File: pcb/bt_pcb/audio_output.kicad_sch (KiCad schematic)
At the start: 34 parts, among them IC1 ADG736BRM, IC2 ADG736BRM, J3 AudioJack3_Switch, J7 AudioJack3_Switch, U2 MCP6004, U4 MCP6004

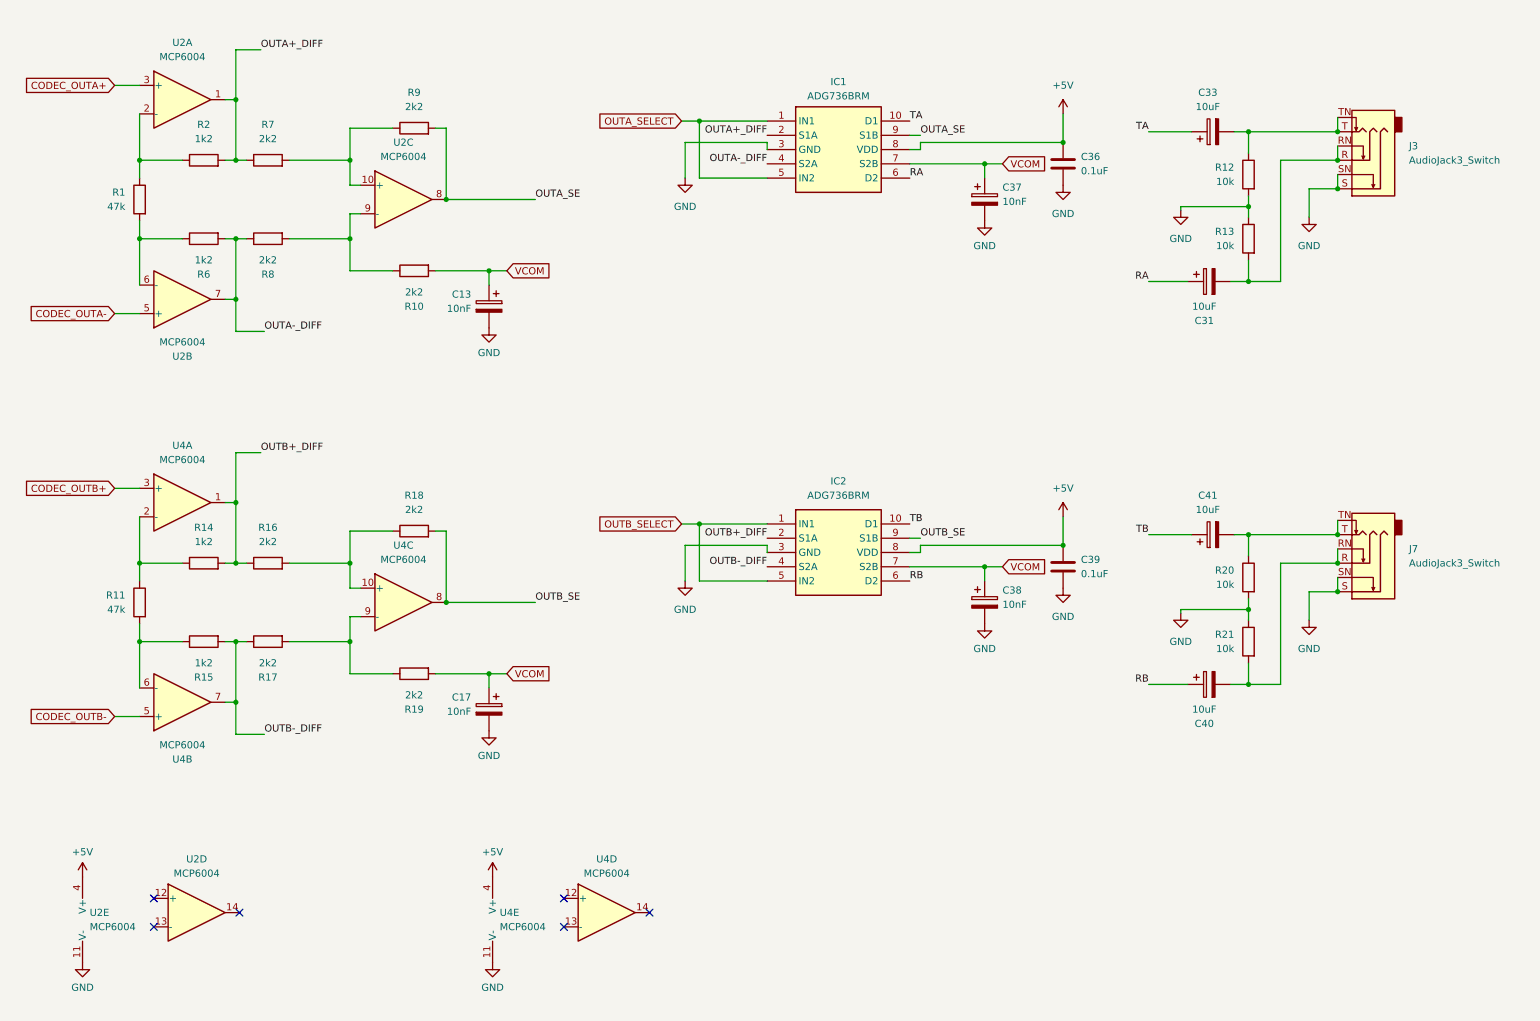
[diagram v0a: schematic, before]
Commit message: ditching power pcb, new codec
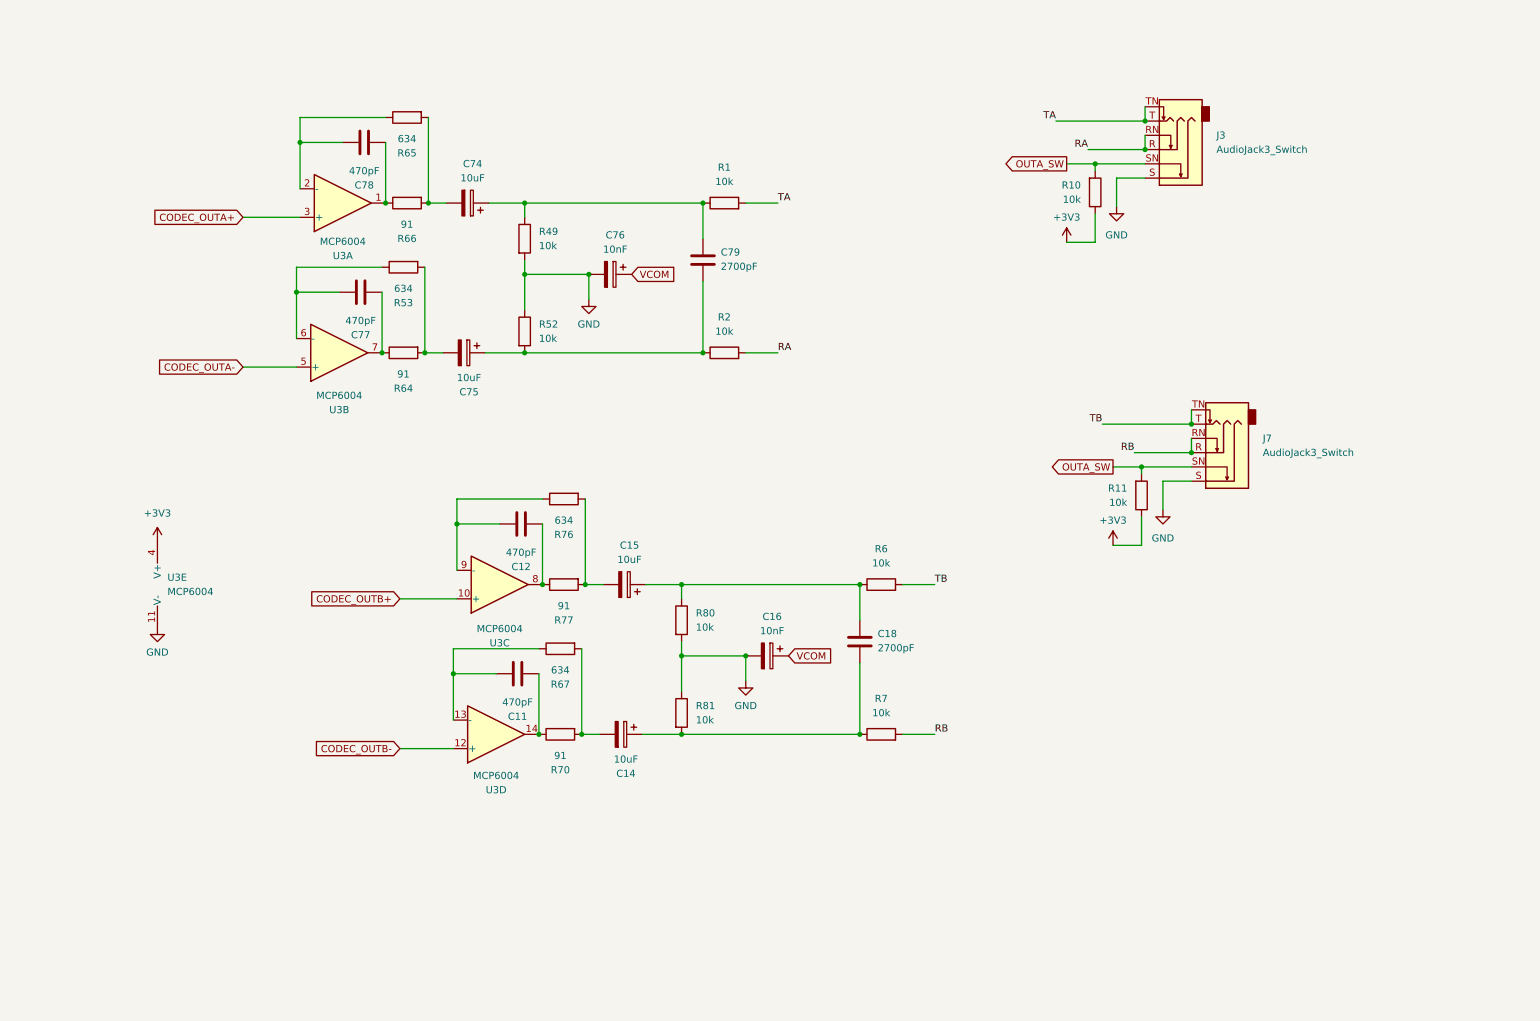
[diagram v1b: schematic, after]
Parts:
- removed C13, C17, C37, C38: 10nF, symbol Device:C_Polarized
- removed C31, C33, C40, C41: 10uF, symbol Device:C_Polarized
- removed C36, C39: 0.1uF, symbol Device:C
- removed IC1, IC2: ADG736BRM, library:SOP50P490X110-10N, symbol library:ADG736BRM
- removed R12, R13, R20, R21: 10k, symbol Device:R
- removed R14, R15: 1k2, symbol Device:R
- removed R16, R17, R18, R19, R8, R9: 2k2, symbol Device:R
- removed U2, U4: MCP6004, symbol Amplifier_Operational:MCP6004
- added C11, C12, C77, C78: 470pF, symbol Device:C
- added C14, C15, C74, C75: 10uF, symbol Device:C_Polarized
- added C16, C76: 10nF, symbol Device:C_Polarized
- added C18, C79: 2700pF, symbol Device:C
- added R49, R52, R80, R81: 10k, symbol Device:R
- added R53, R65, R67, R76: 634, symbol Device:R
- added R64, R66, R70, R77: 91, symbol Device:R
- added U3: MCP6004, symbol Amplifier_Operational:MCP6004
- R1, R11: value 47k -> 10k
- R10, R7: value 2k2 -> 10k
- R2, R6: value 1k2 -> 10k
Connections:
- net OUTA-_DIFF is gone; now on net TB: R6.2
- net CODEC_OUTA+: now also U3.3 (+)
- net CODEC_OUTA-: now also U3.5 (+)
- net CODEC_OUTB+: now also U3.10 (+)
- net CODEC_OUTB-: now also U3.12 (+)
- net GND: now also C16.2, C76.2, R49.2, R52.1, R80.2, R81.1, U3.11 (V-); no longer J3.SN, J7.SN
- net RA: now also J3.R, J3.RN, R2.2
- net RB: now also J7.R, J7.RN, R7.2
- net TA: now also J3.T, J3.TN, R1.2
- net TB: now also J7.T, J7.TN
- net VCOM: now also C16.1, C76.1; no longer R10.2
- net +3V3: now reaches R11.1
- net +3V3: now also R10.1, U3.4 (V+)
- net at R1.1: now also C74.1, C79.1, R49.1; no longer R2.1
- net OUTA_SW: now reaches R11.2
- net OUTA_SW: now also J3.SN, J7.SN, R10.2
- net at R6.1: now also C15.1, C18.1, R80.1; no longer R1.2
- net OUTA+_DIFF: no longer names the net of R7.1
- net OUTA+_DIFF: now also C14.1, C18.2, R81.2; no longer R2.2
- new net: C74.2, R65.2, R66.2
- new net: C77.1, R64.1, U3.7
- new net: C75.2, R53.2, R64.2
- new net: C12.1, R77.1, U3.8
- new net: C12.2, R76.1, U3.9 (-)
- new net: C75.1, C79.2, R2.1, R52.2
- new net: C11.1, R70.1, U3.14
- new net: C11.2, R67.1, U3.13 (-)
- new net: C15.2, R76.2, R77.2
- new net: C14.2, R67.2, R70.2
- new net: C78.1, R66.1, U3.1
- new net: C78.2, R65.1, U3.2 (-)
- new net: C77.2, R53.1, U3.6 (-)
- no-connect marks 6 -> 0
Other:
- moved on the sheet: J3, J7

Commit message: big progress, now revising error and warnings
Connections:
- net +3V3: no longer U3.4 (V+)
- net OUTA_SW: no longer J7.SN, R11.2
- new net +3V3A: U3.4 (V+)
- new net OUTB_SW: J7.SN, R11.2
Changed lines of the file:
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@@
 	)
 	(global_label "OUTA_SW"
-		(shape output)
+		(shape passive)
 		(at 201.295 42.545 180)
 		(fields_autoplaced yes)
@@
 		)
 		(property "Intersheetrefs" "${INTERSHEET_REFS}"
-			(at 189.9641 42.545 0)
+			(at 191.0754 42.545 0)
 			(effects
 				(font
@@
 		)
 	)
-	(global_label "OUTA_SW"
-		(shape output)
+	(global_label "OUTB_SW"
+		(shape passive)
 		(at 209.55 96.52 180)
 		(fields_autoplaced yes)
@@
 		)
 		(property "Intersheetrefs" "${INTERSHEET_REFS}"
-			(at 198.2191 96.52 0)
+			(at 199.149 96.52 0)
 			(effects
 				(font
@@
 				(path "/eb787481-08cd-41a4-a128-173fa6227c32/4ada0139-8712-47ce-9d4c-ab8fef312f7b/92a88d42-e0ca-481e-a77e-2117fd7dfc0f"
 					(reference "C18")
-					(unit 1)
-				)
-			)
-		)
-	)
-	(symbol
-		(lib_id "power:+3V3")
-		(at 39.37 109.855 0)
-		(unit 1)
-		(exclude_from_sim no)
-		(in_bom yes)
-		(on_board yes)
-		(dnp no)
-		(fields_autoplaced yes)
-		(property "Reference" "#PWR027"
-			(at 39.37 113.665 0)
-			(effects
-				(font
-					(size 1.27 1.27)
-				)
-				(hide yes)
-			)
-		)
-		(property "Value" "+3V3"
-			(at 39.37 104.775 0)
-			(effects
-				(font
-					(size 1.27 1.27)
-				)
-			)
-		)
-		(property "Footprint" ""
-			(at 39.37 109.855 0)
-			(effects
-				(font
-					(size 1.27 1.27)
-				)
-				(hide yes)
-			)
-		)
-		(property "Datasheet" ""
-			(at 39.37 109.855 0)
-			(effects
-				(font
-					(size 1.27 1.27)
-				)
-				(hide yes)
-			)
-		)
-		(property "Description" ""
-			(at 39.37 109.855 0)
-			(effects
-				(font
-					(size 1.27 1.27)
-				)
-			)
-		)
-		(pin "1"
-		)
-		(instances
-			(project "bt_pcb"
-				(path "/eb787481-08cd-41a4-a128-173fa6227c32/4ada0139-8712-47ce-9d4c-ab8fef312f7b/92a88d42-e0ca-481e-a77e-2117fd7dfc0f"
-					(reference "#PWR027")
 					(unit 1)
 				)
@@
 					(unit 1)
 				)
+			)
+		)
+	)
+	(symbol
+		(lib_id "power:+3V3")
+		(at 39.37 109.855 0)
+		(unit 1)
+		(exclude_from_sim no)
+		(in_bom yes)
+		(on_board yes)
+		(dnp no)
+		(property "Reference" "#PWR023"
+			(at 39.37 113.665 0)
+			(effects
+				(font
+					(size 1.27 1.27)
+				)
+				(hide yes)
+			)
+		)
+		(property "Value" "+3V3A"
+			(at 39.243 105.029 0)
+			(effects
+				(font
+					(size 1.27 1.27)
+				)
+			)
+		)
+		(property "Footprint" ""
+			(at 39.37 109.855 0)
+			(effects
+				(font
+					(size 1.27 1.27)
+				)
+				(hide yes)
+			)
+		)
+		(property "Datasheet" ""
+			(at 39.37 109.855 0)
+			(effects
+				(font
+					(size 1.27 1.27)
+				)
+				(hide yes)
+			)
+		)
+		(property "Description" ""
+			(at 39.37 109.855 0)
+			(effects
+				(font
+					(size 1.27 1.27)
+				)
+			)
+		)
+		(pin "1"
+		)
+		(instances
+			(project "bt_pcb"
+				(path "/eb787481-08cd-41a4-a128-173fa6227c32/4ada0139-8712-47ce-9d4c-ab8fef312f7b/92a88d42-e0ca-481e-a77e-2117fd7dfc0f"
+					(reference "#PWR023")
+					(unit 1)
+				)

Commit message: solving some erc warnings and errors
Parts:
- renumbered C78 to C62, C77 to C63, C75 to C64, C74 to C65, C12 to C66, C11 to C67, C76 to C68, C14 to C69, C15 to C70, C79 to C71, C16 to C72, C18 to C73, J3 to J15, J7 to J16, R65 to R39, R66 to R40, R53 to R41, R64 to R42, R49 to R43, R52 to R44, R76 to R45, R77 to R46, R67 to R47, R70 to R48, R80 to R49, R81 to R50, R1 to R51, R2 to R52, R6 to R53, R7 to R54, R10 to R55, R11 to R56
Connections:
- net +3V3A renamed +3.3VA
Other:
- moved on the sheet: C62, C63, C65, C67, C68, C69, C70, C71, C72, C73, J15, R41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

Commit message: schematic in theory finished
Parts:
- added R58, R59, R61, R62: 0, Resistor_SMD:R_0603_1608Metric_Pad0.98x0.95mm_HandSolder, symbol Device:R
- C62: value 470pF -> 470p; footprint (none) -> Capacitor_SMD:C_0603_1608Metric_Pad1.08x0.95mm_HandSolder
- C63: renamed from C65; value 10uF -> 10u; footprint (none) -> Capacitor_SMD:C_0805_2012Metric_Pad1.18x1.45mm_HandSolder
- C64: renamed from C71; value 2700pF -> 2.7n; footprint (none) -> Capacitor_SMD:C_0603_1608Metric_Pad1.08x0.95mm_HandSolder
- C65: renamed from C68; value 10nF -> 10n; footprint (none) -> Capacitor_SMD:C_0603_1608Metric_Pad1.08x0.95mm_HandSolder
- C66: renamed from C63; value 470pF -> 470p; footprint (none) -> Capacitor_SMD:C_0603_1608Metric_Pad1.08x0.95mm_HandSolder
- C67: renamed from C64; value 10uF -> 10u; footprint (none) -> Capacitor_SMD:C_0805_2012Metric_Pad1.18x1.45mm_HandSolder
- C68: renamed from C66; value 470pF -> 470p; footprint (none) -> Capacitor_SMD:C_0603_1608Metric_Pad1.08x0.95mm_HandSolder
- C69: renamed from C70; value 10uF -> 10u; footprint (none) -> Capacitor_SMD:C_0805_2012Metric_Pad1.18x1.45mm_HandSolder
- C70: renamed from C73; value 2700pF -> 2.7n; footprint (none) -> Capacitor_SMD:C_0603_1608Metric_Pad1.08x0.95mm_HandSolder
- C71: renamed from C72; value 10nF -> 10n; footprint (none) -> Capacitor_SMD:C_0603_1608Metric_Pad1.08x0.95mm_HandSolder
- C72: renamed from C67; value 470pF -> 470p; footprint (none) -> Capacitor_SMD:C_0603_1608Metric_Pad1.08x0.95mm_HandSolder
- C73: renamed from C69; value 10uF -> 10u; footprint (none) -> Capacitor_SMD:C_0805_2012Metric_Pad1.18x1.45mm_HandSolder
- J13: renamed from J15; value AudioJack3_Switch -> ReanNYS216G; footprint (none) -> library:NYS-216G
- J14: renamed from J16; value AudioJack3_Switch -> ReanNYS216G; footprint (none) -> library:NYS-216G
- R41: renamed from R39; footprint (none) -> Resistor_SMD:R_0603_1608Metric_Pad0.98x0.95mm_HandSolder
- R42: renamed from R40; footprint (none) -> Resistor_SMD:R_0603_1608Metric_Pad0.98x0.95mm_HandSolder
- R43: renamed from R51; footprint (none) -> Resistor_SMD:R_0603_1608Metric_Pad0.98x0.95mm_HandSolder
- R44: renamed from R43; footprint (none) -> Resistor_SMD:R_0603_1608Metric_Pad0.98x0.95mm_HandSolder
- R45: renamed from R41; footprint (none) -> Resistor_SMD:R_0603_1608Metric_Pad0.98x0.95mm_HandSolder
- R46: renamed from R44; footprint (none) -> Resistor_SMD:R_0603_1608Metric_Pad0.98x0.95mm_HandSolder
- R47: renamed from R42; footprint (none) -> Resistor_SMD:R_0603_1608Metric_Pad0.98x0.95mm_HandSolder
- R48: renamed from R52; footprint (none) -> Resistor_SMD:R_0603_1608Metric_Pad0.98x0.95mm_HandSolder
- R49: renamed from R45; footprint (none) -> Resistor_SMD:R_0603_1608Metric_Pad0.98x0.95mm_HandSolder
- R50: renamed from R46; footprint (none) -> Resistor_SMD:R_0603_1608Metric_Pad0.98x0.95mm_HandSolder
- R51: renamed from R53; footprint (none) -> Resistor_SMD:R_0603_1608Metric_Pad0.98x0.95mm_HandSolder
- R52: renamed from R49; footprint (none) -> Resistor_SMD:R_0603_1608Metric_Pad0.98x0.95mm_HandSolder
- R53: renamed from R47; footprint (none) -> Resistor_SMD:R_0603_1608Metric_Pad0.98x0.95mm_HandSolder
- R54: renamed from R50; footprint (none) -> Resistor_SMD:R_0603_1608Metric_Pad0.98x0.95mm_HandSolder
- R55: renamed from R48; footprint (none) -> Resistor_SMD:R_0603_1608Metric_Pad0.98x0.95mm_HandSolder
- R56: renamed from R54; footprint (none) -> Resistor_SMD:R_0603_1608Metric_Pad0.98x0.95mm_HandSolder
- R57: renamed from R55; value 10k -> 47k; footprint (none) -> Resistor_SMD:R_0603_1608Metric_Pad0.98x0.95mm_HandSolder
- R60: renamed from R56; value 10k -> 47k; footprint (none) -> Resistor_SMD:R_0603_1608Metric_Pad0.98x0.95mm_HandSolder
- U3: footprint (none) -> Package_SO:TSSOP-14_4.4x5mm_P0.65mm
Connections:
- net +3V3: now also R57.2, R60.2; no longer R57.1, R60.1
- net GND: now also J13.RN, J13.TN, J14.RN, J14.TN, R59.2, R62.2
- net OUTA_SW: now also R58.2; no longer J13.SN, R57.2
- net OUTB_SW: now also R61.2; no longer J14.SN, R60.2
- net RA: no longer J13.RN
- net RB: no longer J14.RN
- net TA: no longer J13.TN
- net TB: no longer J14.TN
- new net: J14.SN, R60.1, R61.1, R62.1
- new net: J13.SN, R57.1, R58.1, R59.1
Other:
- note added: "In theory: close switch open ground"
- moved on the sheet: C62, C63, C64, C65, C66, C67, C68, C69, C70, C71, C72, C73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

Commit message: pcb started
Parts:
- renumbered J13 to J16, J14 to J17, R41 to R42, R42 to R43, R43 to R44, R44 to R45, R45 to R46, R46 to R47, R47 to R48, R48 to R49, R49 to R50, R50 to R51, R51 to R52, R52 to R53, R53 to R54, R54 to R55, R55 to R56, R56 to R57, R57 to R58, R58 to R59, R59 to R60, R60 to R61, R61 to R62, R62 to R63
